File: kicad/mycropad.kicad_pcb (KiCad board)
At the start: 2 copper layers, 120 x 66 mm, 36 parts, among them M1 MountingHole_2.1mm, M2 MountingHole_2.1mm, M3 MountingHole_2.1mm, M4 MountingHole_2.1mm, M5 MountingHole_2.1mm, M6 MountingHole_2.1mm, SW1 SW_Push, SW2 SW_Push, SW3 SW_Push, SW4 SW_Push, SW5 SW_Push, SW6 SW_Push, SW7 SW_Push, SW8 SW_Push, SW9 RESET, U1 Pico, U2 SN74AHCT125N

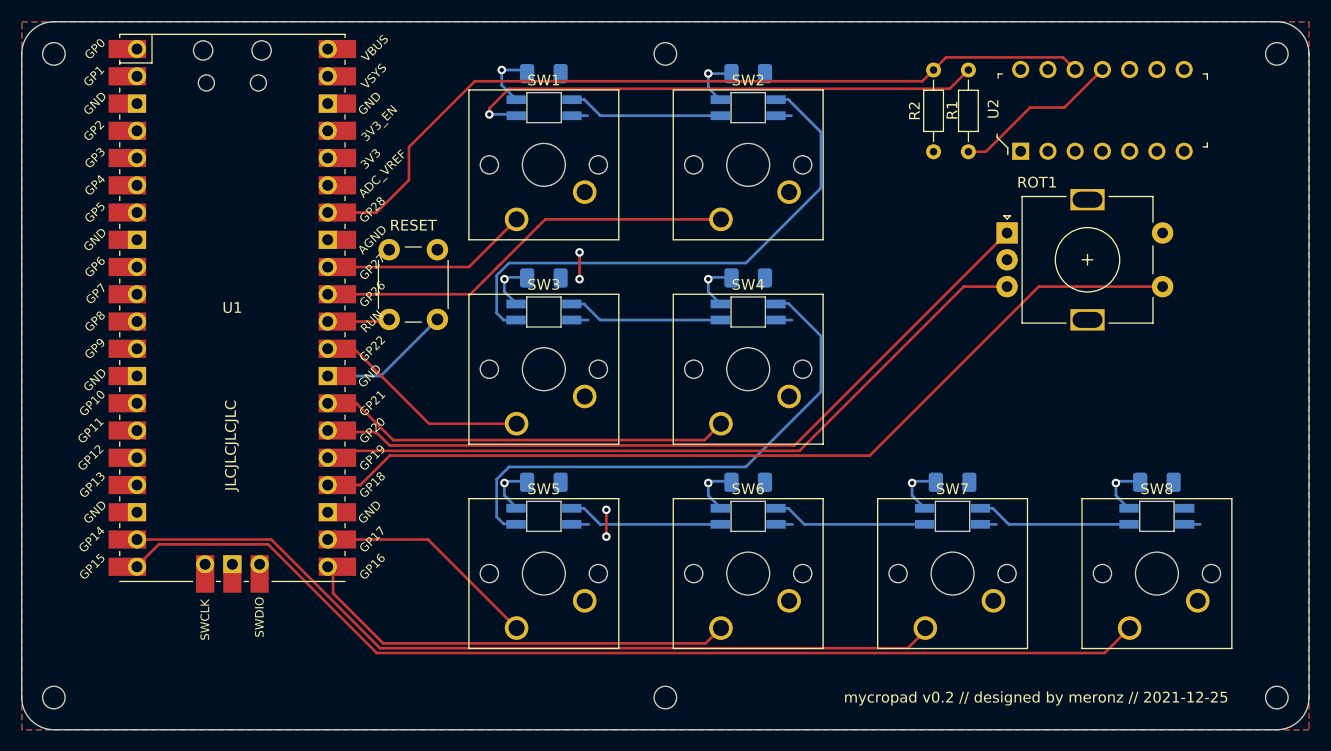
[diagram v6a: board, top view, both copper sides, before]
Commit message: Changed holes position
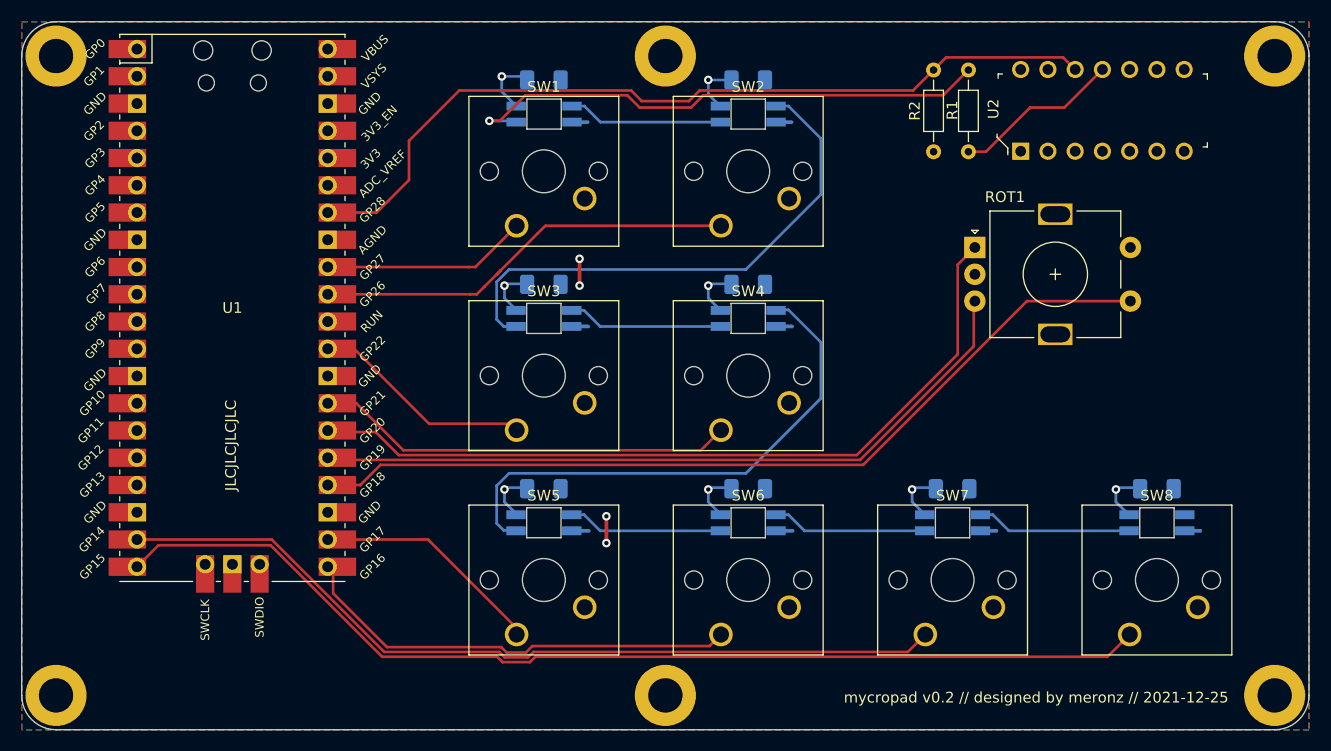
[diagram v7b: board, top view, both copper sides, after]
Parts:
- removed SW9: RESET, Button_Switch_THT:SW_PUSH_6mm_H4.3mm
- M1, M2, M3, M4, M5, M6: value MountingHole_2.1mm -> MountingHole_3.2mm_M3_ISO7380_Pad; footprint MountingHole:MountingHole_2.1mm -> MountingHole:MountingHole_3.2mm_M3_ISO7380_Pad
- moved ROT1 3.29 mm to (160.0, 83.9)
- moved C5 0.60 mm to (119.8, 106.4)
- moved C6 0.60 mm to (138.9, 106.4)
- moved C7 0.60 mm to (157.9, 106.4)
- moved C8 0.60 mm to (177.0, 106.4)
- moved D3 0.60 mm to (119.8, 90.5)
- moved D4 0.60 mm to (138.9, 90.5)
- moved D5 0.60 mm to (119.8, 109.6)
- moved D6 0.60 mm to (138.9, 109.6)
- moved D7 0.60 mm to (157.9, 109.6)
- moved D8 0.60 mm to (177.0, 109.6)
- moved C1 0.60 mm to (119.8, 68.3)
- moved C2 0.60 mm to (138.9, 68.3)
- moved C3 0.60 mm to (119.8, 87.3)
- moved C4 0.60 mm to (138.9, 87.3)
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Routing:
- net GND: track 50.5 -> 38.6 mm
- net RUN: track 5.31 -> 0.00 mm
- net ROT_SW: track 85.5 -> 82.0 mm
- net SW4: track 39.8 -> 37.2 mm
- net ROT_DATA: track 71.6 -> 73.7 mm
- net GPIO28: track 77.4 -> 78.6 mm
- net Net-(D1-Pad4): track 49.1 -> 49.9 mm
- net SW7: track 78.1 -> 78.7 mm
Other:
- outline, holes or cut-outs redrawn
- net class +5v added: clearance 0.2, trace_width 0.35, via_dia 0.8, via_drill 0.4

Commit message: Added owl art to pcb.
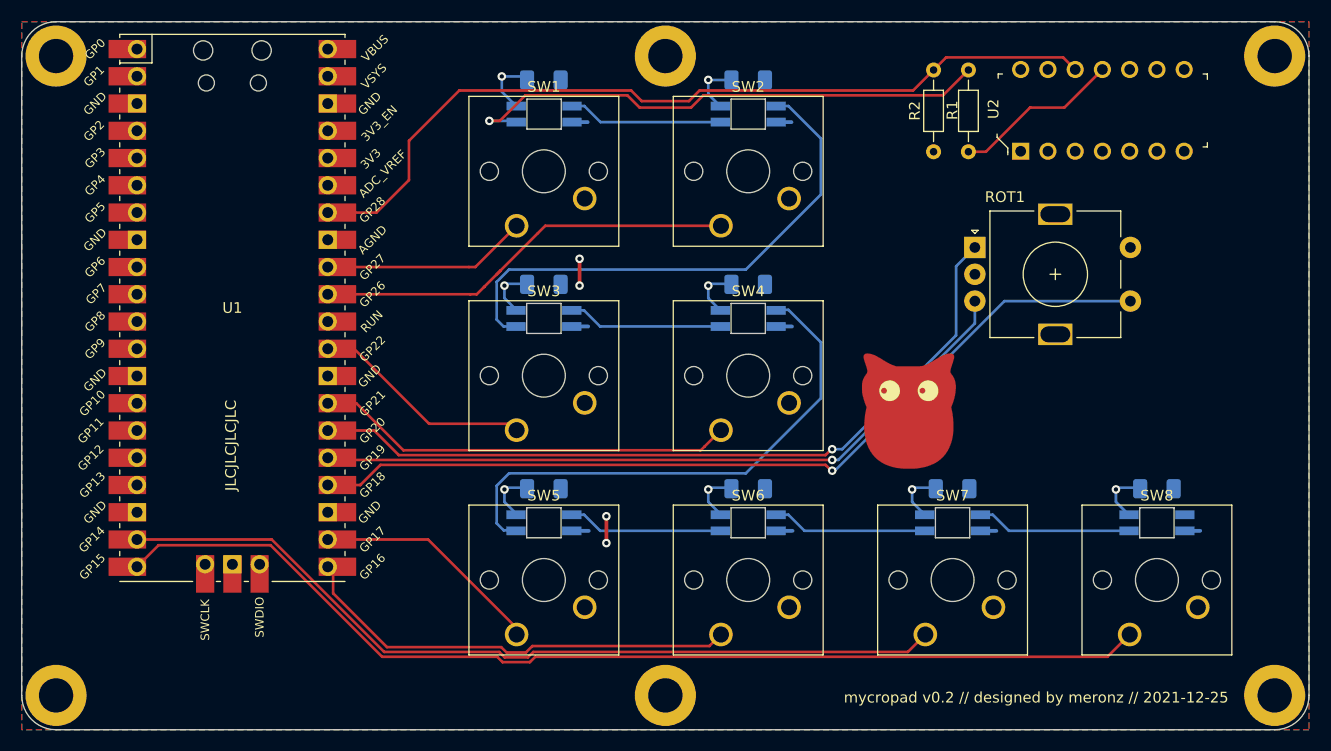
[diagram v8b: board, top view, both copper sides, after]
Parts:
- added Ref**: Val**, mycropad:owl_drawing, F.Cu at (153.9, 99.2)
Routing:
- net ROT_CLK: track 69.9 -> 68.7 mm, vias 0 -> 1
- net ROT_DATA: track 73.7 -> 72.6 mm, vias 0 -> 1
- net ROT_SW: track 82.0 -> 82.4 mm, vias 0 -> 1
